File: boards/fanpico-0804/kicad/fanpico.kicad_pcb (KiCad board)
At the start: 2 copper layers, 135 x 81.5 mm, 164 parts, among them J10 Fan3 Output, J11 Fan4 Output, J12 Fan5 Output, J13 Fan6 Output, J14 Fan7 Output, J15 Fan8 Output, J16 Sensor1, J17 Sensor2, J2 Pico Debug, J3 Floppy Power Connector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

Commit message: PCB version 1.2
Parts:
- added JP10: NTC Value, Connector_PinHeader_2.54mm:PinHeader_1x03_P2.54mm_Vertical, F.Cu at (79.9, 67.0)
- added JP11: NTC Value, Connector_PinHeader_2.54mm:PinHeader_1x03_P2.54mm_Vertical, F.Cu at (88.8, 67.0)
- added R52: 100k, Resistor_SMD:R_0603_1608Metric_Pad0.98x0.95mm_HandSolder, F.Cu at (77.4, 59.5)
- added R53: 100k, Resistor_SMD:R_0603_1608Metric_Pad0.98x0.95mm_HandSolder, F.Cu at (96.4, 63.5)
- added TP6: TestPoint, TestPoint:TestPoint_Pad_D1.5mm, F.Cu at (101.8, 72.8)
- added TP7: TestPoint, TestPoint:TestPoint_Pad_D1.5mm, F.Cu at (113.2, 72.8)
- added TP8: TestPoint, TestPoint:TestPoint_Pad_D1.5mm, F.Cu at (124.8, 72.8)
- added TP9: TestPoint, TestPoint:TestPoint_Pad_D1.5mm, F.Cu at (136.8, 72.8)
- C30, C5, C7, C8: footprint Capacitor_SMD:C_1206_3216Metric_Pad1.33x1.80mm_HandSolder -> Capacitor_Tantalum_SMD:CP_EIA-3216-18_Kemet-A_Pad1.58x1.35mm_HandSolder
- J16, J17: footprint Connector_JST:JST_PH_B2B-PH-K_1x02_P2.00mm_Vertical -> Connector_JST:JST_XH_B2B-XH-A_1x02_P2.50mm_Vertical
- R3, R48: value 300 -> 330
- moved R50 6.96 mm to (77.4, 63.1), turned to -90 degrees
- moved C6 6.62 mm to (83.1, 71.4), turned to -90 degrees
- moved R51 5.38 mm to (96.4, 59.8), turned to -90 degrees
- moved JP1 5.35 mm to (67.2, 63.0)
- moved U5 4.02 mm to (87.8, 74.2), turned to -90 degrees
- moved J16 1.76 mm to (81.3, 58.6)
- moved D3 1.50 mm to (75.0, 71.8)
- moved J17 1.50 mm to (90.0, 58.6)
- moved C5 1.00 mm to (69.5, 76.2)
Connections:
- R50 pad 2: ADC_REF -> Net-(JP10-Pad1)
- R51 pad 2: ADC_REF -> Net-(JP11-Pad1)
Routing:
- net GND: track 370.8 -> 333.5 mm, vias 78 -> 77
- net FAN2_TACHO_GEN: track 63.9 -> 80.0 mm
- net Net-(JP10-Pad3): track 0.00 -> 15.0 mm
- net FAN1_PWR: track 166.0 -> 179.6 mm
- net Net-(JP11-Pad1): track 0.00 -> 12.5 mm
- net AGND: track 87.1 -> 98.7 mm
- net Net-(C7-Pad1): track 22.0 -> 32.2 mm
- net FAN4_PWR: track 105.5 -> 114.8 mm
- net FAN3_PWR: track 125.5 -> 134.8 mm
- net FAN2_PWR: track 126.9 -> 136.0 mm
- net 3V3: track 456.1 -> 464.3 mm
- net Net-(C5-Pad1): track 26.6 -> 18.6 mm
- net TEMP2_READ: track 74.7 -> 81.1 mm
- net TEMP1_READ: track 63.5 -> 68.9 mm
- net Net-(JP11-Pad3): track 0.00 -> 4.16 mm
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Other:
- board text added: "100k"
- board text added: "10k"
- board text added: "FanPico v1.2 by Timo Kokkonen <tjko@iki.fi> 2022-03-11 github.com/tjko/fanpico"
- board text removed: "FanPico v1.1 by Timo Kokkonen <tjko@iki.fi> 2022-02-26"

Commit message: New PCB revision v1.3
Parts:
- C30, C7, C8: value 10uF 15V -> 10uF 16V
- SW1: footprint Button_Switch_THT:SW_PUSH_6mm -> Button_Switch_THT:SW_PUSH_6mm_SMD_2
- moved C24 10.9 mm to (162.3, 102.5)
- moved C22 10.8 mm to (162.3, 113.8)
- moved C26 10.7 mm to (162.3, 91.1)
- moved C28 10.6 mm to (162.3, 79.8)
- moved C11 9.30 mm to (101.1, 124.6)
- moved C14 9.30 mm to (112.7, 124.7)
- moved C17 9.20 mm to (136.0, 124.7)
- moved C20 9.10 mm to (124.5, 124.7)
- moved J8 7.78 mm to (100.3, 129.9), turned to 0 degrees
- moved J10 7.66 mm to (123.4, 129.9), turned to 0 degrees
- moved J14 7.62 mm to (167.4, 90.3), turned to 90 degrees
- moved J4 7.62 mm to (108.1, 59.6), turned to 180 degrees
- moved J5 7.62 mm to (119.6, 59.6), turned to 180 degrees
- moved J6 7.62 mm to (131.1, 59.6), turned to 180 degrees
- moved J7 7.62 mm to (142.6, 59.6), turned to 180 degrees
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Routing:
- net GND: track 333.5 -> 213.7 mm
- net /Fan Channels/Fan3/PWM_OUT: track 18.9 -> 29.8 mm
- net /Fan Channels/Fan2/PWM_OUT: track 19.4 -> 30.2 mm
- net /Fan Channels/Fan1/PWM_OUT: track 19.0 -> 29.9 mm
- net /Fan Channels/Fan4/PWM_OUT: track 19.6 -> 30.2 mm
- net /Fan Channels/Fan3/PWM_IN: track 6.05 -> 14.6 mm
- net /Fan Channels/Fan2/PWM_IN: track 6.09 -> 14.7 mm
- net /Fan Channels/Fan6/PWM_OUT: track 18.8 -> 27.3 mm, vias 0 -> 2
- net /Fan Channels/Fan7/PWR_OUT: track 35.4 -> 27.0 mm
- net /Fan Channels/Fan4/PWM_IN: track 6.74 -> 15.0 mm
- net /Fan Channels/Fan5/PWM_OUT: track 18.3 -> 26.6 mm, vias 0 -> 2
- net /Fan Channels/Fan1/PWM_IN: track 6.36 -> 14.6 mm
- net /Fan Channels/Fan6/PWR_OUT: track 35.3 -> 27.4 mm
- net /Fan Channels/Fan3/TACHO_IN: track 29.8 -> 22.3 mm
- net /Fan Channels/Fan2/TACHO_IN: track 29.6 -> 22.2 mm
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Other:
- board text added: "DEBUG"
- board text added: "FanPico v1.3 by Timo Kokkonen <tjko@iki.fi> 2022-04-11 github.com/tjko/fanpico"
- board text added: "RESET"
- board text removed: "FanPico v1.2 by Timo Kokkonen <tjko@iki.fi> 2022-03-11 github.com/tjko/fanpico"
- board text removed: "Reset"

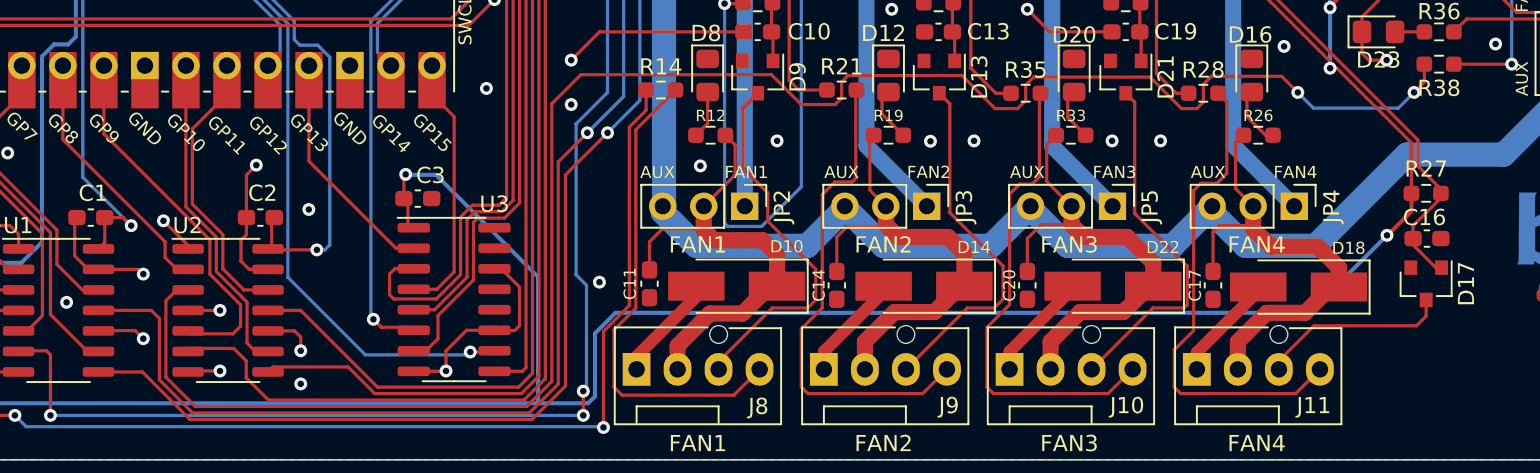
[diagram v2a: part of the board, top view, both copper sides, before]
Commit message: Cleanup schematic (no actual changes that affect PCB).
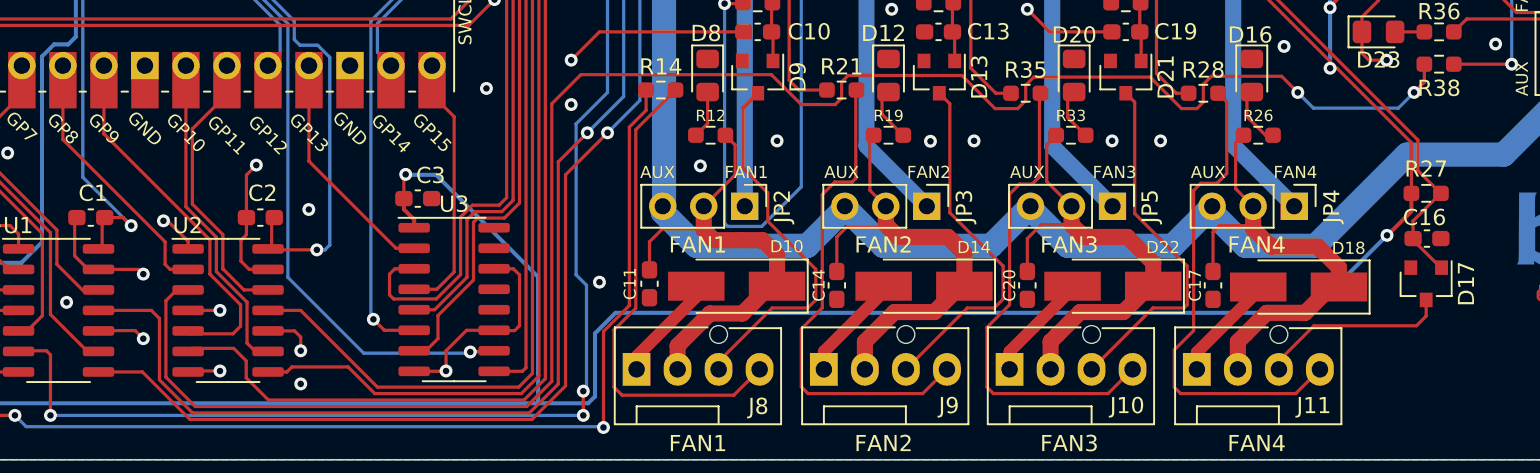
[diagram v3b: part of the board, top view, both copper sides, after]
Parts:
- J4: value Fan1 Input -> MB Fan1 Input
- J5: value Fan2 Input -> MB Fan2 Input
- J6: value Fan3 Input -> MB Fan3 Input
- J7: value Fan4 Input -> MB Fan4 Input
- U3: footprint Package_SO:SOP-16_3.9x9.9mm_P1.27mm -> Package_SO:SOIC-16_3.9x9.9mm_P1.27mm
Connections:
- net FAN1_PWM_READ renamed MBFAN1_PWM_READ
- net FAN1_TACHO_GEN renamed MBFAN1_TACHO_GEN
- net FAN2_PWM_READ renamed MBFAN2_PWM_READ
- net FAN2_TACHO_GEN renamed MBFAN2_TACHO_GEN
- net FAN3_PWM_READ renamed MBFAN3_PWM_READ
- net FAN3_TACHO_GEN renamed MBFAN3_TACHO_GEN
- net FAN4_PWM_READ renamed MBFAN4_PWM_READ
- net FAN4_TACHO_GEN renamed MBFAN4_TACHO_GEN
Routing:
- net GND: track 213.7 -> 214.3 mm
- net 3V3: track 465.2 -> 465.8 mm
